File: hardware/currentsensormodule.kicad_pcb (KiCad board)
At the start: 2 copper layers, 92 x 59.7 mm, 105 parts, among them J101 USART, J102 STLink, J103 Sensor1, J104 Sensor2, J105 RJ45, J106 RJ45, U101 LM324, U103 K78L15-1000R3, U104 K78L15-1000R3, U105 AMS1117-5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

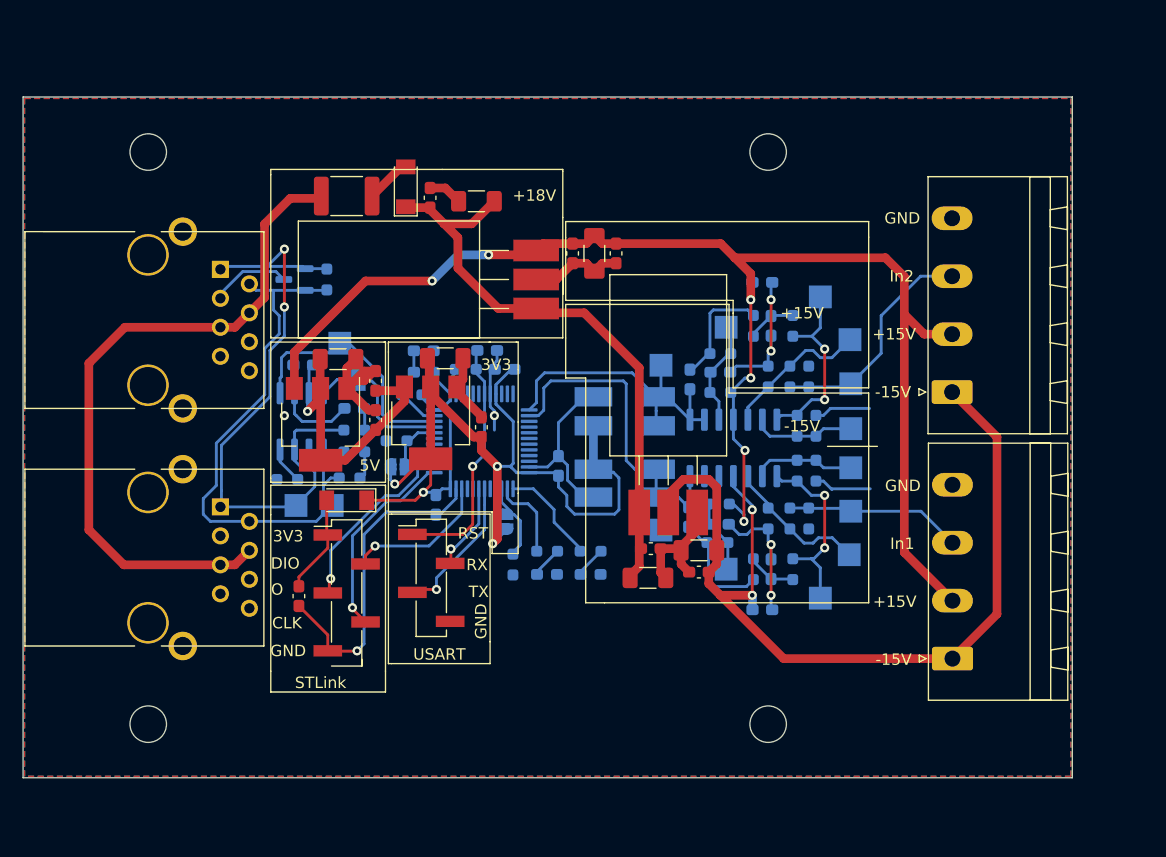
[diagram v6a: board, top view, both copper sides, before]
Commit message: hardware: PCB size adjust
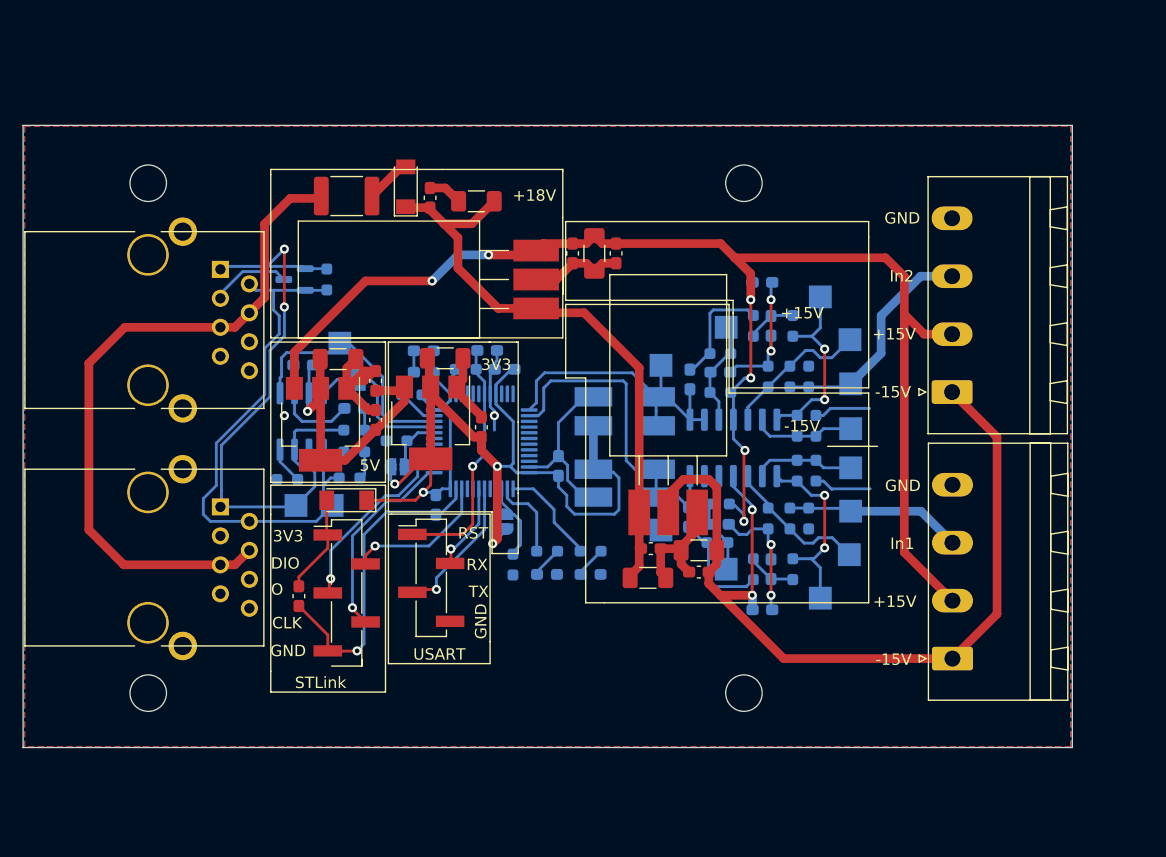
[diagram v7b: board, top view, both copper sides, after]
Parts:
- moved H103 3.46 mm to (152.7, 77.4)
- moved H104 3.45 mm to (152.7, 122.1)
- moved H102 2.73 mm to (100.5, 77.4)
- moved H101 2.72 mm to (100.5, 122.1)
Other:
- board size 92 x 59.7 mm -> 92 x 54.5 mm
- board text added: "6cm"
- board text added: "9,2cm"
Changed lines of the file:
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@@
   )
   (footprint "MountingHole:MountingHole_3.2mm_M3" (layer "F.Cu")
-    (at 154.813 124.841)
+    (at 152.69 122.12)
     (descr "Mounting Hole 3.2mm, no annular, M3")
     (tags "mounting hole 3.2mm no annular m3")
@@
   )
   (footprint "MountingHole:MountingHole_3.2mm_M3" (layer "F.Cu")
-    (at 100.457 124.841)
+    (at 100.457 122.12)
     (descr "Mounting Hole 3.2mm, no annular, M3")
     (tags "mounting hole 3.2mm no annular m3")
@@
   )
   (footprint "MountingHole:MountingHole_3.2mm_M3" (layer "F.Cu")
-    (at 154.813 74.676)
+    (at 152.69 77.41)
     (descr "Mounting Hole 3.2mm, no annular, M3")
     (tags "mounting hole 3.2mm no annular m3")
@@
   )
   (footprint "MountingHole:MountingHole_3.2mm_M3" (layer "F.Cu")
-    (at 100.457 74.676)
+    (at 100.457 77.41)
     (descr "Mounting Hole 3.2mm, no annular, M3")
     (tags "mounting hole 3.2mm no annular m3")
@@
   (gr_line (start 121.5136 103.2764) (end 121.5136 106.1212) (layer "F.SilkS") (width 0.12))
   (gr_line (start 163.6268 80.772) (end 163.6268 82.1436) (layer "F.SilkS") (width 0.12))
-  (gr_arc (start 159.303128 76.535872) (mid 154.813 74.676) (end 152.953128 70.185872) (layer "Dwgs.User") (width 0.1))
-  (gr_arc (start 152.908 129.286) (mid 154.767872 124.795872) (end 159.258 122.936) (layer "Dwgs.User") (width 0.1))
   (gr_poly
     (pts
-      (xy 181.483 129.54)
-      (xy 89.4842 129.54)
-      (xy 89.4842 69.85)
-      (xy 181.483 69.85)
+      (xy 181.483 126.89)
+      (xy 89.4842 126.89)
+      (xy 89.4842 72.34)
+      (xy 181.483 72.34)
     ) (layer "Edge.Cuts") (width 0.05) (fill none))
   (gr_text "GND" (at 166.0144 80.4672) (layer "B.SilkS")
@@
     (effects (font (size 1 1) (thickness 0.15)))
   )
+  (gr_text "6cm" (at 69.2404 103.3272) (layer "Dwgs.User")
+    (effects (font (size 5 5) (thickness 0.15)))
+  )
+  (gr_text "9,2cm" (at 134.9248 143.4084) (layer "Dwgs.User")
+    (effects (font (size 5 5) (thickness 0.15)))
+  )
+  (dimension (type aligned) (layer "Dwgs.User")
+    (pts (xy 177.08 72.42) (xy 177.08 77.41))
+    (height 24.39)
+    (gr_text "4.9900 mm" (at 151.54 74.915 90) (layer "Dwgs.User")
+      (effects (font (size 1 1) (thickness 0.15)))
+    )
+    (format (units 3) (units_format 1) (precision 4))
+    (style (thickness 0.1) (arrow_length 1.27) (text_position_mode 0) (extension_height 0.58642) (extension_offset 0.5) keep_text_aligned)
+  )
   (dimension (type aligned) (layer "Dwgs.User")
     (pts (xy 181.483 129.54) (xy 89.789 129.54))
     (height -7.366)
-    (gr_text "3610.0000 mils" (at 135.636 133.756) (layer "Dwgs.User")
+    (gr_text "91.6940 mm" (at 135.636 133.756) (layer "Dwgs.User")
       (effects (font (size 3 3) (thickness 0.15)))
     )
@@
   )
   (dimension (type aligned) (layer "Dwgs.User")
-    (pts (xy 89.789 69.85) (xy 89.789 129.54))
-    (height 5.461)
-    (gr_text "2350.0000 mils" (at 81.178 99.695 90) (layer "Dwgs.User")
-      (effects (font (size 3 3) (thickness 0.15)))
+    (pts (xy 181.5 123.16) (xy 181.5 76.39))
+    (height 2.26)
+    (gr_text "46.7700 mm" (at 182.61 99.775 90) (layer "Dwgs.User")
+      (effects (font (size 1 1) (thickness 0.15)))
     )
     (format (units 3) (units_format 1) (precision 4))
@@
   )
   (dimension (type aligned) (layer "Dwgs.User")
-    (pts (xy 175.641 76.454) (xy 175.641 71.374))
+    (pts (xy 152.69 121.82) (xy 152.69 132.08))
     (height 0)
-    (gr_text "200.0000 mils" (at 174.491 73.914 90) (layer "Dwgs.User")
+    (gr_text "10.2600 mm" (at 151.54 126.95 90) (layer "Dwgs.User")
       (effects (font (size 1 1) (thickness 0.15)))
     )
@@
   )
   (dimension (type aligned) (layer "Dwgs.User")
-    (pts (xy 159.258 129.286) (xy 154.813 124.841))
-    (height 0)
-    (gr_text "247.4874 mils" (at 157.848673 126.250327 -45) (layer "Dwgs.User")
+    (pts (xy 177.08 121.82) (xy 177.08 126.81))
+    (height 24.39)
+    (gr_text "4.9900 mm" (at 151.54 124.315 90) (layer "Dwgs.User")
       (effects (font (size 1 1) (thickness 0.15)))
     )
@@
   )
   (dimension (type aligned) (layer "Dwgs.User")
-    (pts (xy 159.303128 70.185872) (xy 154.858128 74.630872))
-    (height 0)
-    (gr_text "247.4874 mils" (at 156.267455 71.595199 45) (layer "Dwgs.User")
+    (pts (xy 181.48 126.83) (xy 181.48 72.45))
+    (height 4.96)
+    (gr_text "54.3800 mm" (at 185.29 99.64 90) (layer "Dwgs.User")
       (effects (font (size 1 1) (thickness 0.15)))
     )
@@
   )
   (dimension (type aligned) (layer "Dwgs.User")
-    (pts (xy 175.641 128.27) (xy 175.641 123.19))
+    (pts (xy 152.69 77.41) (xy 152.69 67.15))
     (height 0)
-    (gr_text "200.0000 mils" (at 174.491 125.73 90) (layer "Dwgs.User")
+    (gr_text "10.2600 mm" (at 151.54 72.28 90) (layer "Dwgs.User")
+      (effects (font (size 1 1) (thickness 0.15)))
+    )
+    (format (units 3) (units_format 1) (precision 4))
+    (style (thickness 0.1) (arrow_length 1.27) (text_position_mode 0) (extension_height 0.58642) (extension_offset 0.5) keep_text_aligned)
+  )
+  (dimension (type aligned) (layer "Eco1.User")
+    (pts (xy 181.55 132.12) (xy 181.55 67.15))
+    (height 7.25)
+    (gr_text "64.9700 mm" (at 187.65 99.635 90) (layer "Eco1.User")
+      (effects (font (size 1 1) (thickness 0.15)))
+    )
+    (format (units 3) (units_format 1) (precision 4))
+    (style (thickness 0.1) (arrow_length 1.27) (text_position_mode 0) (extension_height 0.58642) (extension_offset 0.5) keep_text_aligned)
+  )
+  (dimension (type aligned) (layer "Eco1.User")
+    (pts (xy 181.46 129.45) (xy 177.07 129.45))
+    (height 0)
+    (gr_text "4.3900 mm" (at 179.265 128.3) (layer "Eco1.User")
+      (effects (font (size 1 1) (thickness 0.15)))
+    )
+    (format (units 3) (units_format 1) (precision 4))
+    (style (thickness 0.1) (arrow_length 1.27) (text_position_mode 0) (extension_height 0.58642) (extension_offset 0.5) keep_text_aligned)
+  )
+  (dimension (type aligned) (layer "Eco1.User")
+    (pts (xy 177.06 72.4) (xy 177.06 67.15))
+    (height -4.430007)
+    (gr_text "5.2500 mm" (at 171.479993 69.775 90) (layer "Eco1.User")
+      (effects (font (size 1 1) (thickness 0.15)))
+    )
+    (format (units 3) (units_format 1) (precision 4))
+    (style (thickness 0.1) (arrow_length 1.27) (text_position_mode 0) (extension_height 0.58642) (extension_offset 0.5) keep_text_aligned)
+  )
+  (dimension (type aligned) (layer "Eco1.User")
+    (pts (xy 181.45 72.45) (xy 177.06 72.45))
+    (height 0)
+    (gr_text "4.3900 mm" (at 179.255 71.3) (layer "Eco1.User")
+      (effects (font (size 1 1) (thickness 0.15)))
+    )
+    (format (units 3) (units_format 1) (precision 4))
+    (style (thickness 0.1) (arrow_length 1.27) (text_position_mode 0) (extension_height 0.58642) (extension_offset 0.5) keep_text_aligned)
+  )
+  (dimension (type aligned) (layer "Eco1.User")
+    (pts (xy 176.93 132.08) (xy 176.93 126.83))
+    (height -4.430007)
+    (gr_text "5.2500 mm" (at 171.349993 129.455 90) (layer "Eco1.User")
       (effects (font (size 1 1) (thickness 0.15)))
     )
@@
   (segment (start 162.052 106.172) (end 161.798 105.918) (width 0.254) (layer "B.Cu") (net 28))
   (segment (start 161.798 105.918) (end 158.3925 105.918) (width 0.254) (layer "B.Cu") (net 28))
-  (segment (start 168.214 106.172) (end 170.9745 108.9325) (width 0.254) (layer "B.Cu") (net 28))
+  (segment (start 168.214 106.172) (end 170.9745 108.9325) (width 0.762) (layer "B.Cu") (net 28))
   (segment (start 156.718 105.8945) (end 158.369 105.8945) (width 0.254) (layer "B.Cu") (net 28))
   (segment (start 158.3925 105.918) (end 158.369 105.8945) (width 0.254) (layer "B.Cu") (net 28))
-  (segment (start 162.052 106.172) (end 168.214 106.172) (width 0.254) (layer "B.Cu") (net 28))
+  (segment (start 162.052 106.172) (end 168.214 106.172) (width 0.762) (layer "B.Cu") (net 28))
   (segment (start 161.7745 95.2735) (end 162.052 94.996) (width 0.254) (layer "B.Cu") (net 29))
   (segment (start 158.369 95.2735) (end 156.718 95.2735) (width 0.254) (layer "B.Cu") (net 29))
-  (segment (start 164.719 92.329) (end 164.719 89.027) (width 0.254) (layer "B.Cu") (net 29))
-  (segment (start 162.052 94.996) (end 164.719 92.329) (width 0.254) (layer "B.Cu") (net 29))
-  (segment (start 168.1815 85.5645) (end 170.942 85.5645) (width 0.254) (layer "B.Cu") (net 29))
+  (segment (start 164.719 92.329) (end 164.719 89.027) (width 0.762) (layer "B.Cu") (net 29))
+  (segment (start 162.052 94.996) (end 164.719 92.329) (width 0.762) (layer "B.Cu") (net 29))
+  (segment (start 168.1815 85.5645) (end 170.942 85.5645) (width 0.762) (layer "B.Cu") (net 29))
   (segment (start 158.369 95.2735) (end 161.7745 95.2735) (width 0.254) (layer "B.Cu") (net 29))
-  (segment (start 164.719 89.027) (end 168.1815 85.5645) (width 0.254) (layer "B.Cu") (net 29))
+  (segment (start 164.719 89.027) (end 168.1815 85.5645) (width 0.762) (layer "B.Cu") (net 29))
   (segment (start 154.305 103.095) (end 154.305 102.362) (width 0.254) (layer "B.Cu") (net 30))
   (segment (start 154.9635 101.7035) (end 157.353 101.7035) (width 0.254) (layer "B.Cu") (net 30))
@@
   (segment (start 116.106 105.2068) (end 116.106 108.1598) (width 0.254) (layer "F.Cu") (net 69))
   (zone (net 1) (net_name "GND") (layers F&B.Cu) (hatch edge 0.508)
-    (connect_pads (clearance 0.254))
+    (connect_pads yes (clearance 0.254))
     (min_thickness 0.254) (filled_areas_thickness no)
     (fill yes (thermal_gap 0.508) (thermal_bridge_width 0.508))
     (polygon
       (pts
-        (xy 181.356 129.413)
-        (xy 89.6112 129.413)
-        (xy 89.6112 69.977)
-        (xy 181.356 69.977)
+        (xy 181.356 126.823)
+        (xy 89.6112 126.823)
+        (xy 89.6112 72.417)
+        (xy 181.356 72.417)
       )
     )

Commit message: hardware: fixed RJ45 footp sh pin, added shapes3D (including K78L15)
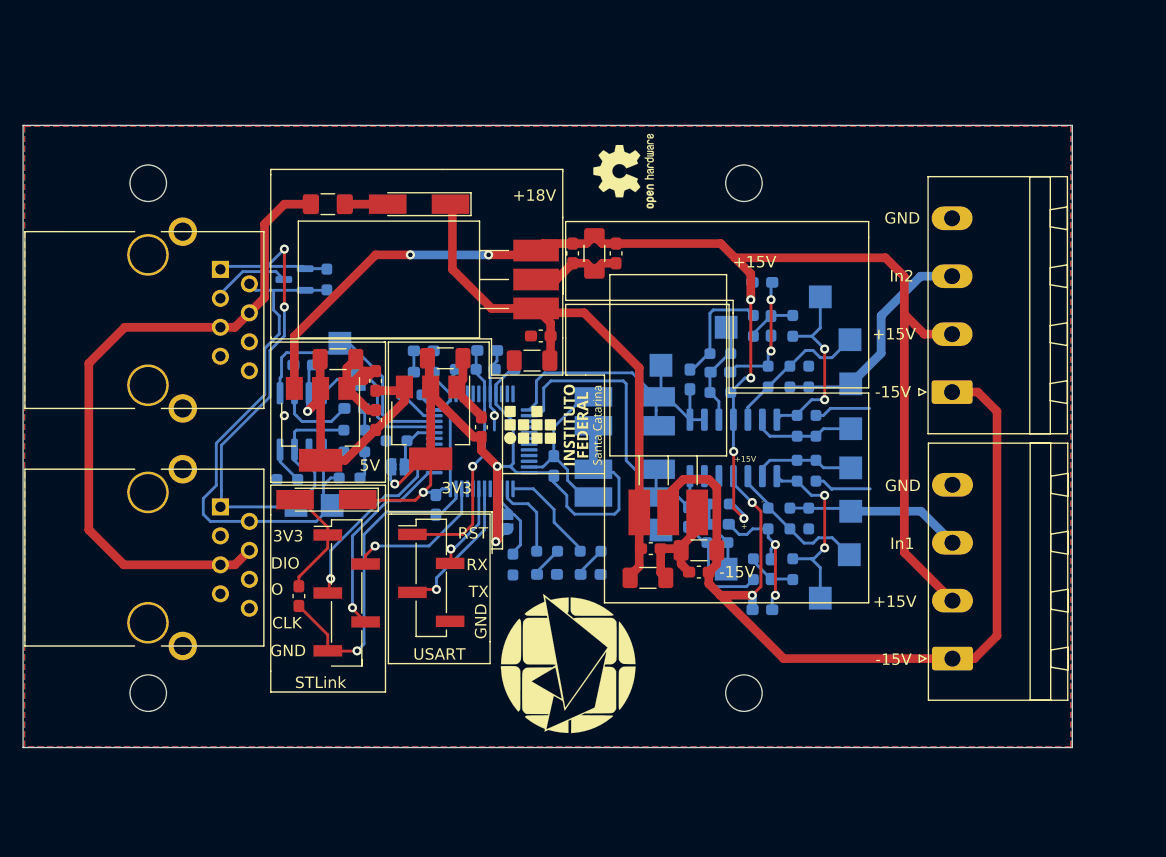
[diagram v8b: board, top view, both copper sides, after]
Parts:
- added LOGO101: Logo_Open_Hardware_Small, Symbol:OSHW-Logo2_7.3x6mm_SilkScreen, F.Cu at (142.2, 76.4)
- added SYM101: SYM_Radioactive_Radiation_Small, logo:logo, F.Cu at (137.3, 119.5)
- added SYM102: SYM_LASER_Small, logoifsc:logoifsc, F.Cu at (135.9, 98.6)
- added SYM103: SYM_Radioactive_Radiation_Small, logo:logo, B.Cu at (125.2, 83.5)
- added SYM104: SYM_LASER_Small, logoifsc:logoifsc, B.Cu at (137.2, 83.1)
- D108, D109: footprint Diode_SMD:D_MiniMELF -> Diode_SMD:D_MiniMELF_Handsoldering
- F101: footprint Fuse:Fuse_1812_4532Metric_Pad1.30x3.40mm_HandSolder -> Fuse:Fuse_1206_3216Metric_Pad1.42x1.75mm_HandSolder
- R107, R110: value 1k -> 560
- R108, R109: value 3k9 -> 560
- R117, R118: value 15k -> 22k
- moved C119 15.5 mm to (134.9, 90.8), turned to 0 degrees
- moved C117 14.8 mm to (134.1, 93.0)
- moved D108 1.92 mm to (124.2, 79.2), turned to 180 degrees
- moved F101 1.80 mm to (116.2, 79.2)
- moved D109 1.78 mm to (116.1, 105.2)
- moved C112 0.41 mm to (136.0, 102.2)
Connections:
- J105 pad 9: (no net) -> GND
- J106 pad 9: (no net) -> GND
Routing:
- net -15V: track 81.3 -> 84.4 mm
- net GND: track 150.7 -> 148.1 mm
- net /POWER SUPPLY/+18V: track 52.0 -> 49.6 mm
- net Net-(C101-Pad2): track 8.63 -> 10.1 mm
- net /CANBUS CONN/CAN_18V: track 60.7 -> 59.5 mm
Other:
- board text added: "+"
- board text added: "-"
- board text added: "5,44 cm"
- board text added: "9,17 cm"
- board text removed: "6cm"
- board text removed: "9,2cm"
